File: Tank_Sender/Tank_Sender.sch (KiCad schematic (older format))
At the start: 12 parts, among them J101 Interface, J102 TANK, J103 TANK, U101 H7550-H#

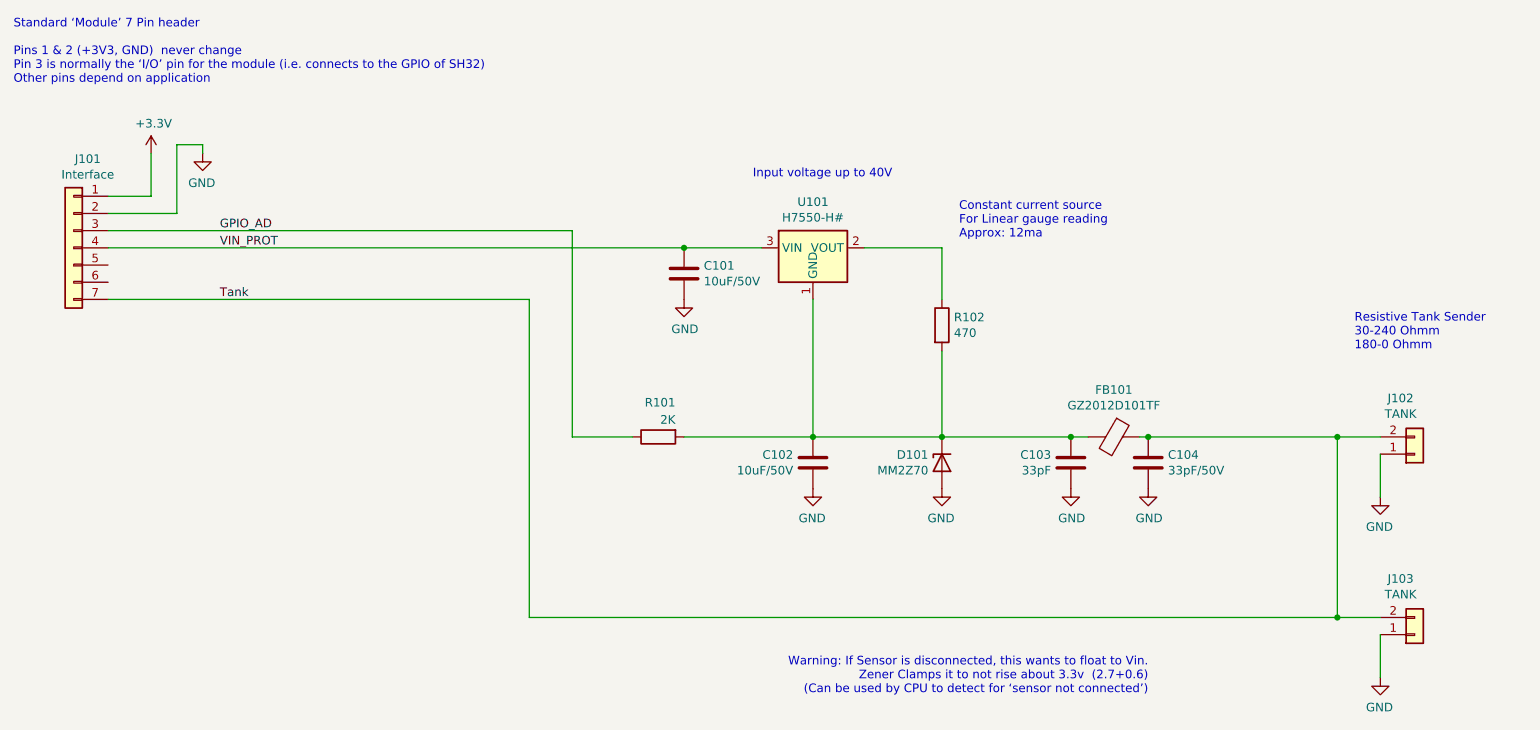
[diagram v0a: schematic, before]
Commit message: New GND Pin.  Added PI Filters to all inputs.    Refined Layout
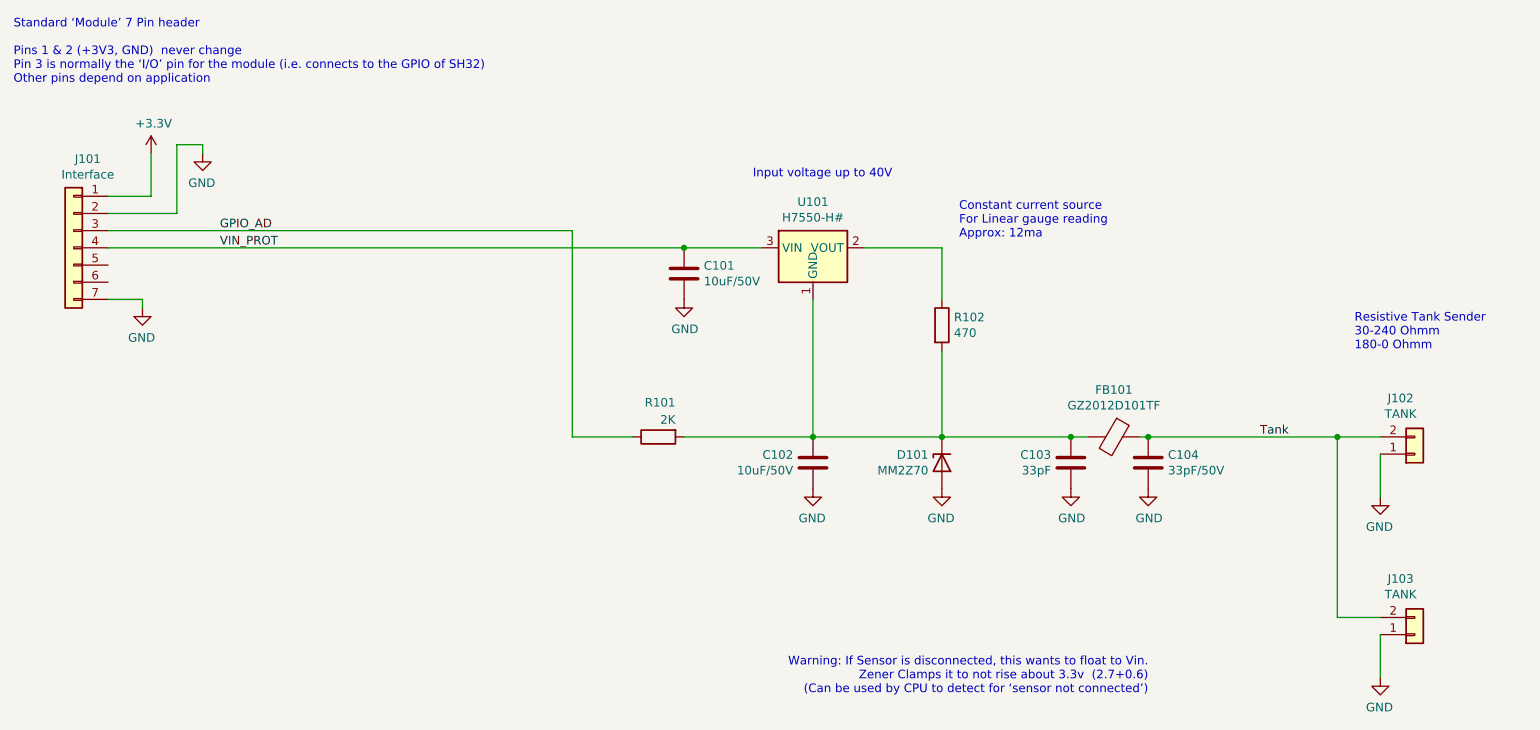
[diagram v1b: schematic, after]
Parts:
- D101: LCSC C118617 -> (none)
- R101, R102: footprint Resistor_SMD:R_1206_3216Metric -> Resistor_SMD:R_0603_1608Metric
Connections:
- net GND: now also J101.7 (Pin_7)
- net Tank: no longer J101.7 (Pin_7)
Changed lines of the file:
@@
 F 0 "R102" H 6520 3196 50  0000 L CNN
 F 1 "470" H 6520 3105 50  0000 L CNN
-F 2 "Resistor_SMD:R_1206_3216Metric" V 6380 3150 50  0001 C CNN
+F 2 "Resistor_SMD:R_0603_1608Metric" V 6380 3150 50  0001 C CNN
 F 3 "~" H 6450 3150 50  0001 C CNN
 F 4 "" H 6450 3150 50  0001 C CNN "LCSC"
@@
 F 2 "Diode_SMD:D_SOD-323" H 6450 3950 50  0001 C CNN
 F 3 "" H 6450 3950 50  0001 C CNN
-F 4 "C118617" H 6450 3950 50  0001 C CNN "LCSC"
+F 4 "" H 6450 3950 50  0001 C CNN "LCSC"
 	1    6450 3950
 	0    -1   1    0
@@
 F 0 "R101" V 4600 3700 50  0000 L CNN
 F 1 "2K" V 4700 3700 50  0000 L CNN
-F 2 "Resistor_SMD:R_1206_3216Metric" V 4730 3800 50  0001 C CNN
+F 2 "Resistor_SMD:R_0603_1608Metric" V 4730 3800 50  0001 C CNN
 F 3 "~" H 4800 3800 50  0001 C CNN
 F 4 "" H 4800 3800 50  0001 C CNN "LCSC"
@@
 Connection ~ 6450 3800
 Wire Wire Line
-	6450 3800 7200 3800
-Wire Wire Line
 	4950 3800 5700 3800
 $Comp
@@
 Connection ~ 7650 3800
 Wire Wire Line
-	8750 4850 8750 3800
-Wire Wire Line
-	7650 3800 8750 3800
-Connection ~ 8750 3800
-Wire Wire Line
-	8750 3800 9000 3800
-Wire Wire Line
 	4300 3800 4650 3800
-Wire Wire Line
-	4050 4850 8750 4850
 $Comp
 L power:GND #PWR0107
@@
 Text Label 2250 2700 0    50   ~ 0
 VIN_PROT
-Wire Wire Line
-	4050 4850 4050 3000
-Wire Wire Line
-	4050 3000 1600 3000
-Text Label 2250 3000 0    50   ~ 0
+Text Label 8300 3800 0    50   ~ 0
 Tank
 $Comp
@@
 	-1   0    0    -1
 $EndComp
-Connection ~ 8750 4850
-Wire Wire Line
-	9000 4850 8750 4850
 $Comp
 L power:GND #PWR0109
@@
 	1    0    0    1
 $EndComp
+$Comp
+L power:GND #PWR0110
+U 1 1 5FBFFD61
+P 1800 3050
+AR Path="/5FBFFD61" Ref="#PWR0110"  Part="1"
+AR Path="/5C3476D8/5FBFFD61" Ref="#PWR?"  Part="1"
+AR Path="/5CA65CC5/5FBFFD61" Ref="#PWR?"  Part="1"
+AR Path="/5F6FAF6E/5FBFFD61" Ref="#PWR?"  Part="1"
+AR Path="/5FB0E40B/5FBFFD61" Ref="#PWR?"  Part="1"
+AR Path="/5FB12AF7/5FBFFD61" Ref="#PWR?"  Part="1"
+F 0 "#PWR0110" H 1800 2800 50  0001 C CNN
+F 1 "GND" H 1805 2877 50  0000 C CNN
+F 2 "" H 1800 3050 50  0001 C CNN
+F 3 "" H 1800 3050 50  0001 C CNN
+	1    1800 3050
+	-1   0    0    -1
+$EndComp
+Wire Wire Line
+	1600 3000 1800 3000
+Wire Wire Line
+	1800 3000 1800 3050
+Wire Wire Line
+	8750 3800 9000 3800
+Wire Wire Line
+	7650 3800 8750 3800
+Connection ~ 8750 3800
+Wire Wire Line
+	9000 4850 8750 4850
+Wire Wire Line
+	8750 4850 8750 3800
+Wire Wire Line
+	6450 3800 7200 3800
 $EndSCHEMATC

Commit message: Fix Symbol Libraries
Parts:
- U101: symbol SH-ESP32:HT75xx-1-SOT23 -> YachtHardware:HT75xx-1-SOT23
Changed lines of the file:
@@
 	4950 3800 5700 3800
 $Comp
-L SH-ESP32:HT75xx-1-SOT23 U?
+L YachtHardware:HT75xx-1-SOT23 U?
 U 1 1 5FB238C7
 P 5700 2800

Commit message: Opto - LCSC Parts added
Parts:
- D101: value MM2Z70 -> KDZ3.3V-RTK/P; LCSC (none) -> C155470
- R101: LCSC (none) -> C22975
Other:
- note added: "Warning: If Sensor is disconnected, this wants to float to Vin.\nZener Clamps it to not rise about 3.3v \n(Can be used by CPU to detect for ‘sensor not connected’)"
- note removed: "Warning: If Sensor is disconnected, this wants to float to Vin.\nZener Clamps it to not rise about 3.3v (2.7+0.6)\n(Can be used by CPU to detect for ‘sensor not connected’)"
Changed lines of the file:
@@
 AR Path="/5FB12AF7/5FB2385B" Ref="D?"  Part="1"
 F 0 "D101" V 6404 4029 50  0000 L CNN
-F 1 "MM2Z70" V 6495 4029 50  0000 L CNN
+F 1 "KDZ3.3V-RTK/P" V 6495 4029 50  0000 L CNN
 F 2 "Diode_SMD:D_SOD-323" H 6450 3950 50  0001 C CNN
-F 3 "" H 6450 3950 50  0001 C CNN
-F 4 "" H 6450 3950 50  0001 C CNN "LCSC"
+F 3 "https://datasheet.lcsc.com/szlcsc/KEC-Semicon-KDZ3-3V-RTK-P_C155470.pdf" H 6450 3950 50  0001 C CNN
+F 4 "C155470" H 6450 3950 50  0001 C CNN "LCSC"
 	1    6450 3950
 	0    -1   1    0
@@
 F 2 "Resistor_SMD:R_0603_1608Metric" V 4730 3800 50  0001 C CNN
 F 3 "~" H 4800 3800 50  0001 C CNN
-F 4 "" H 4800 3800 50  0001 C CNN "LCSC"
+F 4 "C22975" H 4800 3800 50  0001 C CNN "LCSC"
 	1    4800 3800
 	0    -1   1    0
@@
 Constant current source\nFor Linear gauge reading\nApprox: 12ma
 Text Notes 7650 5300 2    50   ~ 0
-Warning: If Sensor is disconnected, this wants to float to Vin.\nZener Clamps it to not rise about 3.3v  (2.7+0.6)\n(Can be used by CPU to detect for ‘sensor not connected’)
+Warning: If Sensor is disconnected, this wants to float to Vin.\nZener Clamps it to not rise about 3.3v  \n(Can be used by CPU to detect for ‘sensor not connected’)
 $Comp
 L Device:C C103
